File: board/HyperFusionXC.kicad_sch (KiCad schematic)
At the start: 142 parts, among them J1 Conn_01x03, J2 10067847-001RLF, J3 UJ20-C-H-G-SMT-2-P16-TR, J4 UJ20-C-H-G-SMT-2-P16-TR, J5 Conn_01x08, J6 Conn_01x05, J7 Conn_02x05_Odd_Even, Q1 UM6K34NTCN, U1 SOM_FPGA_LP, U10 SN74LVC1G04DCKR, U11 AP22816BKAWT-7, U12 TXS0108EPWR, U14 TXS0108EPWR, U15 TXB0104D, U2 74AHC541, U3 74AHC541, U4 MAX3814, U5 NAU88C22A, U6 ESP32-S3-WROOM-1-N8R8, U7 MCP2221AT-I/SL, U8 74AHC541, U9 AP22816BKAWT-7, X1 EDGE50/MSX, X2 SS-53000-001, X3 490107671012_JTAG

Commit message: Routing done
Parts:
- added C55: 100nF, Capacitor_SMD:C_0603_1608Metric, symbol Device:C_Small
- added C56: 4.7uF, Capacitor_SMD:C_0603_1608Metric, symbol Device:C_Small
- C105: value 4.7uF -> 100nF; DIGIKEY 1276-2087-1-ND -> 311-1088-1-ND; LCSC C107368 -> (none)
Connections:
- net +5V: now also C55.2, C56.2
- net GND: now also C55.1, C56.1
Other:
- moved on the sheet: C1, X1

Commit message: Improvements
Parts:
- added R41, R42, R51, R52: 2k2, Resistor_SMD:R_0603_1608Metric, symbol Device:R_Small
- AX1, AX2: LCSC (none) -> C20182914
- C1, C23, C25, C28, C29, C36, C39, C40, C54, C56: LCSC C107368 -> C1952593
- C10, C105, C11, C12, C13, C14, C16, C17, C19, C2, C20, C21, C24, C26, C3, C31, C37, C38, C4, C42, C43, C44, C45, C46, C47, C5, C53, C55, C6, C7, C8, C9: LCSC (none) -> C109474
- C103, C27, C30, C33, C34, C35, C41, C48, C49, C50, C51, C52: LCSC (none) -> C309479
- C15, C18, C22: value 4.7uF -> 1uF; DIGIKEY 1276-2087-1-ND -> 4988-NMC0603X7R105K6.3TRPFCT-ND; LCSC C107368 -> C309479
- C32: value 100nF -> 1uF; DIGIKEY 311-1088-1-ND -> 4988-NMC0603X7R105K6.3TRPFCT-ND; LCSC (none) -> C309479
- FL1, FL2: LCSC (none) -> C882594
- J2: LCSC (none) -> C569097
- LED1: LCSC (none) -> C6784997
- MP1: LCSC (none) -> C9900196740
- Q1: LCSC (none) -> C510056
- R1, R11, R12, R2, R26, R35, R36, R37, R38, R39, R50: LCSC (none) -> C25804
- R10, R20, R21, R22, R23, R24, R7, R8, R9: LCSC (none) -> C22775
- R13: LCSC (none) -> C23024
- R14, R15, R16, R17, R18, R19, R25, R3, R4, R5, R6: LCSC (none) -> C8218
- R27, R28, R29, R30, R31, R32, R33, R34: LCSC (none) -> C4275
- R40, R43, R44, R72: LCSC (none) -> C21190
- R45: LCSC (none) -> C22962
- R46, R47, R48, R49: LCSC (none) -> C23186
- U1: LCSC (none) -> C22426477
- U10: value SN74LVC1G04DCKR -> SN74LVC1G04DBVR; DIGIKEY 296-11600-1-N -> 296-11599-1-ND; LCSC (none) -> C7827
- U11, U9: LCSC (none) -> C3236237
- U12, U14: LCSC (none) -> C17206
- U15: LCSC (none) -> C1549752
- U2, U3, U8: DIGIKEY (none) -> 1727-3994-1-ND; LCSC (none) -> C282411
- U4: LCSC (none) -> C117541
- U5: LCSC (none) -> C914209
- U6: LCSC (none) -> C2913201
- U7: LCSC (none) -> C626750
- VR1: LCSC (none) -> C22038443
- X2: LCSC (none) -> C7017495
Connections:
- net +3V3: now also C15.1, R51.1, R52.1; no longer C15.2
- net ESP_IO17/SCL: now also R51.2
- net ESP_IO18/SDA: now also R52.2
- net GND: now also C15.2; no longer C15.1
- net at C51.1, U5.4 (RMICP): now also R42.2
- net at C29.1, U5.32 (MICBIAS): now also R41.1, R42.1
- net at C49.1, U5.1 (LMICP): now also R41.2
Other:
- moved on the sheet: C24, C29, C36, C49, C51, Q1A, Q1B, R12, R37, R38, R43, R44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

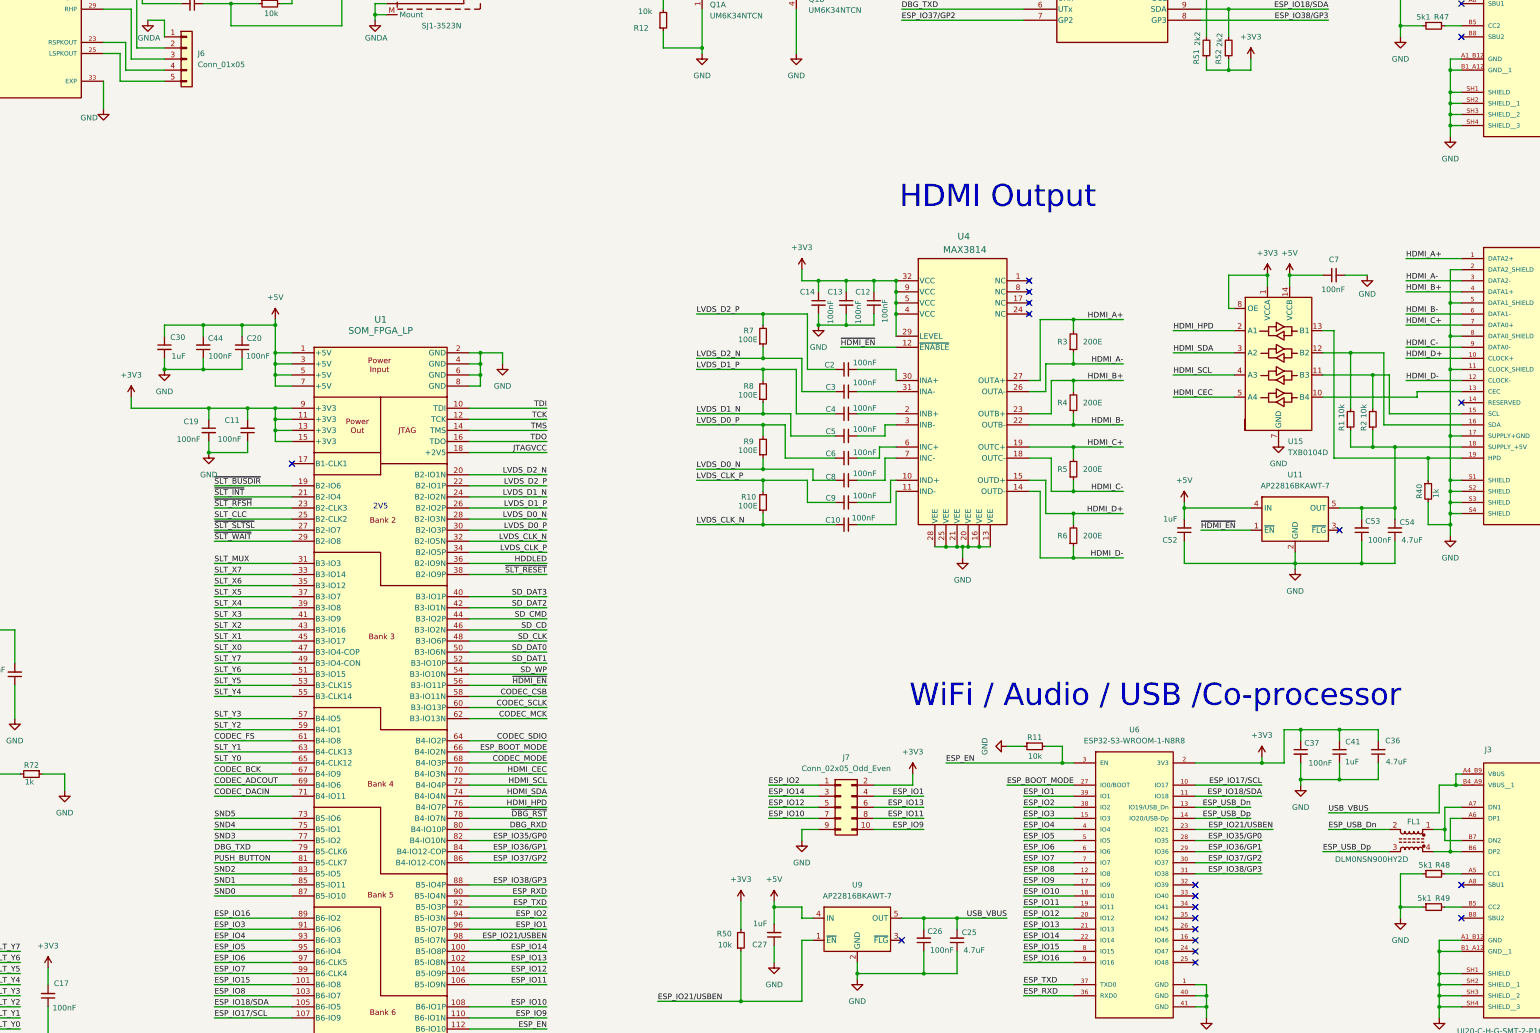
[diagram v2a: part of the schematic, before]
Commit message: Redesigned HDMI to solve obsolescence
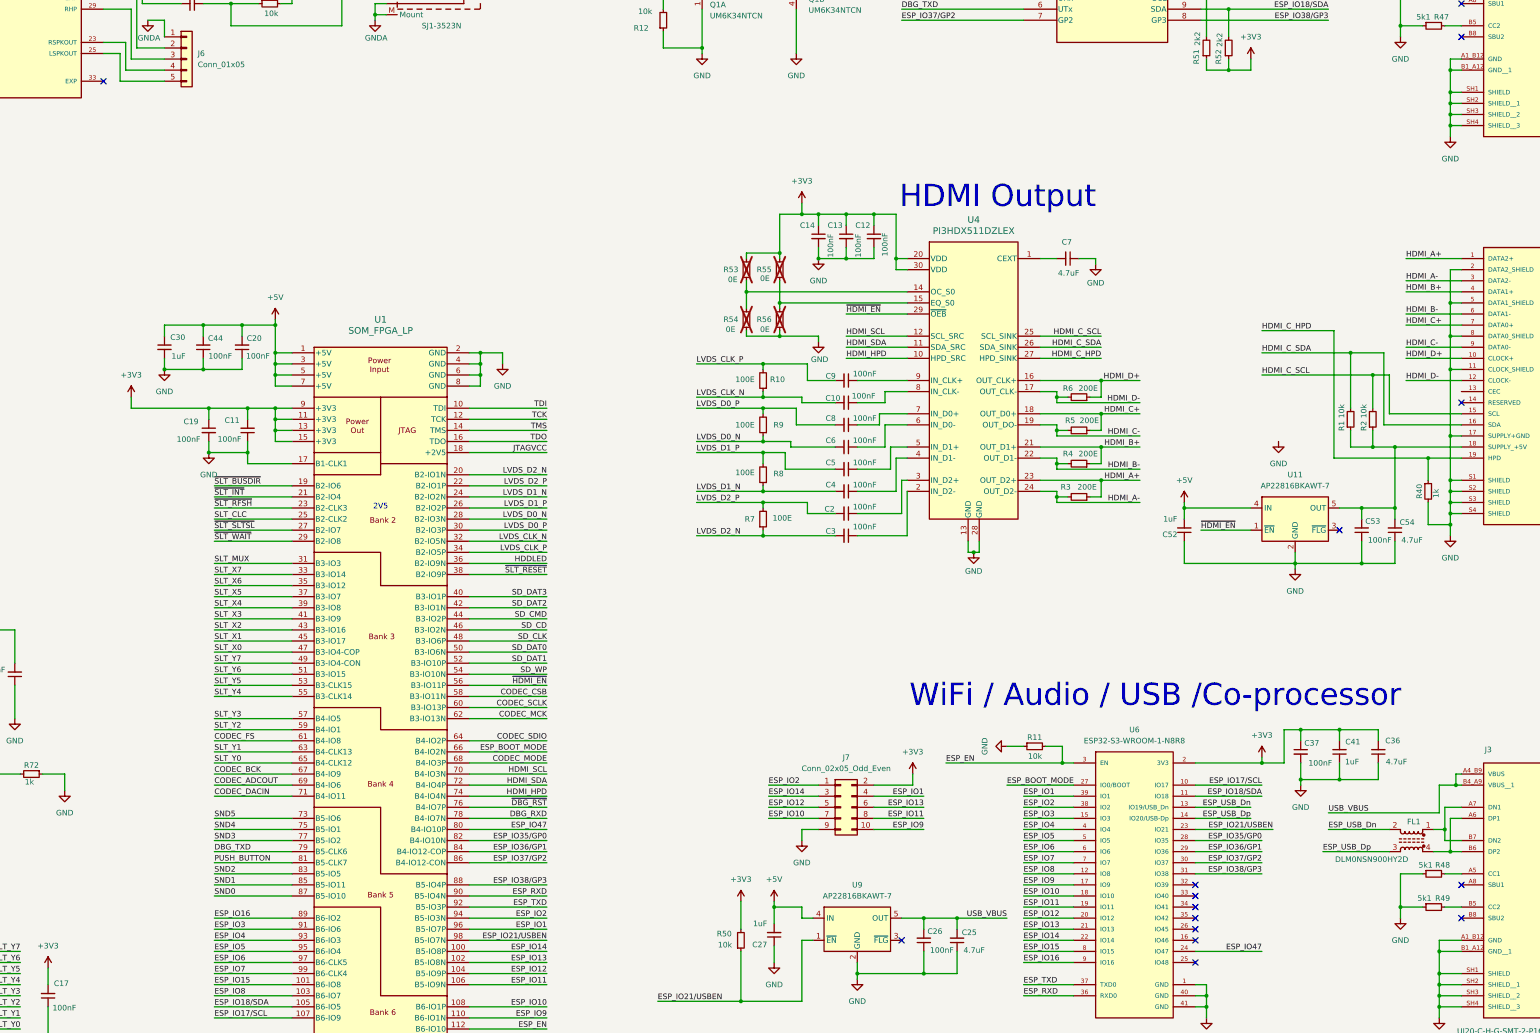
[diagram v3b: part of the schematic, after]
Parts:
- removed U15: TXB0104D, Package_SO:SOIC-14_3.9x8.7mm_P1.27mm, symbol Logic_LevelTranslator:TXB0104D
- removed U4: MAX3814, Package_QFP:TQFP-32_5x5mm_P0.5mm, symbol Library:MAX3814
- added R53, R54, R55, R56: 0E, Resistor_SMD:R_0603_1608Metric, symbol Device:R_Small
- added U4: PI3HDX511DZLEX, Package_DFN_QFN:Texas_RNH0030A_WQFN-30-1EP_2.5x4.5mm_P0.4mm_EP1.2x3.2mm, symbol Library:PI3HDX511DZLEX
- C7: value 100nF -> 4.7uF; DIGIKEY 311-1088-1-ND -> 1276-2087-1-ND; LCSC C109474 -> C1952593
- U5: footprint Library:QFN-32-NAU88C22YG -> Library:QFN-32-1EP_5x5mm_P0.5mm_EP2.7x2.7mm_ThermalVias
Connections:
- net HDMI_CEC is gone; now on net HDMI_SCL: U1.70 (B4-IO3N)
- net +3V3: now also R53.1, R55.1, U4.20 (VDD), U4.30 (VDD)
- net +5V: no longer C7.1
- net DBG_RXD: now also U1.78 (B4-IO7N); no longer U1.80 (B4-IO10P)
- net GND: now also C7.1, U1.17 (B1-CLK1), R54.2, R56.2, U4.13 (GND), U4.28 (GND); no longer C7.2, U5.33 (EXP)
- net HDMI_A+: now also R3.1, U4.23 (OUT_D2+); no longer R3.2
- net HDMI_A-: now also R3.2, U4.24 (OUT_D2-); no longer R3.1
- net HDMI_B+: now also R4.1, U4.21 (OUT_D1+); no longer R4.2
- net HDMI_B-: now also R4.2, U4.22 (OUT_D1-); no longer R4.1
- net HDMI_C+: now also R5.1, U4.18 (OUT_D0+); no longer R5.2
- net HDMI_C-: now also R5.2, U4.19 (OUT_DO-); no longer R5.1
- net HDMI_D+: now also R6.1, U4.16 (OUT_CLK+); no longer R6.2
- net HDMI_D-: now also R6.2, U4.17 (OUT_CLK-); no longer R6.1
- net HDMI_HPD: now also U1.74 (B4-IO4N), U4.10 (HPD_SRC); no longer U1.76 (B4-IO7P)
- net HDMI_SCL: now also U4.12 (SCL_SRC); no longer U1.72 (B4-IO4P)
- net HDMI_SDA: now also U1.72 (B4-IO4P), U4.11 (SDA_SRC); no longer U1.74 (B4-IO4N)
- net LVDS_D0_N: now also C6.2; no longer C8.2
- net LVDS_D0_P: now also C8.2; no longer C6.2
- net LVDS_D1_N: now also C4.2; no longer C5.2
- net LVDS_D1_P: now also C5.2; no longer C4.2
- net ~{DBG_RST}: now also U1.76 (B4-IO7P); no longer U1.78 (B4-IO7N)
- net ~{HDMI_EN}: now also U4.29 (~{OEB})
- net at C3.1: now also U4.2 (IN_D2-)
- net HDMI_C_SDA: now reaches R1.2, X2.16 (SDA)
- net HDMI_C_SDA: now also U4.26 (SDA_SINK)
- net at C8.1: now also U4.7 (IN_D0+)
- net at C5.1: now also U4.5 (IN_D1+)
- net at C10.1: now also U4.8 (IN_CLK-)
- net at C4.1: now also U4.4 (IN_D1-)
- net at C2.1: now also U4.3 (IN_D2+)
- net HDMI_C_HPD: now reaches R40.1, X2.19 (HPD)
- net HDMI_C_HPD: now also U4.27 (HPD_SINK)
- net ESP_IO47: now reaches U6.24 (IO47)
- net ESP_IO47: now also U1.80 (B4-IO10P)
- net HDMI_C_SCL: now reaches R2.2, X2.15 (SCL)
- net HDMI_C_SCL: now also U4.25 (SCL_SINK)
- net at C6.1: now also U4.6 (IN_D0-)
- net at C9.1: now also U4.9 (IN_CLK+)
- new net: C7.2, U4.1 (CEXT)
- new net: R53.2, R54.1, U4.14 (OC_S0)
- new net: R55.2, R56.1, U4.15 (EQ_S0)
- no-connect marks 29 -> 24
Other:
- moved on the sheet: C10, C12, C13, C14, C2, C3, C4, C5, C6, C8, C9, R10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
